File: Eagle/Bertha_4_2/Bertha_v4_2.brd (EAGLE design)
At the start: 100 x 84.6 mm, 117 parts, among them CON1 JACK_DC_BARREL, IC1 MCP1703DB, IC3 SN74LVC2G14, J1 RJ12RIGHTANGLE-I2C, J2 RJ12RIGHTANGLE-I2C, J7 22--02, Q1 BSP75, Q2 BSP75, Q3 BSP75, Q4 BSP75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

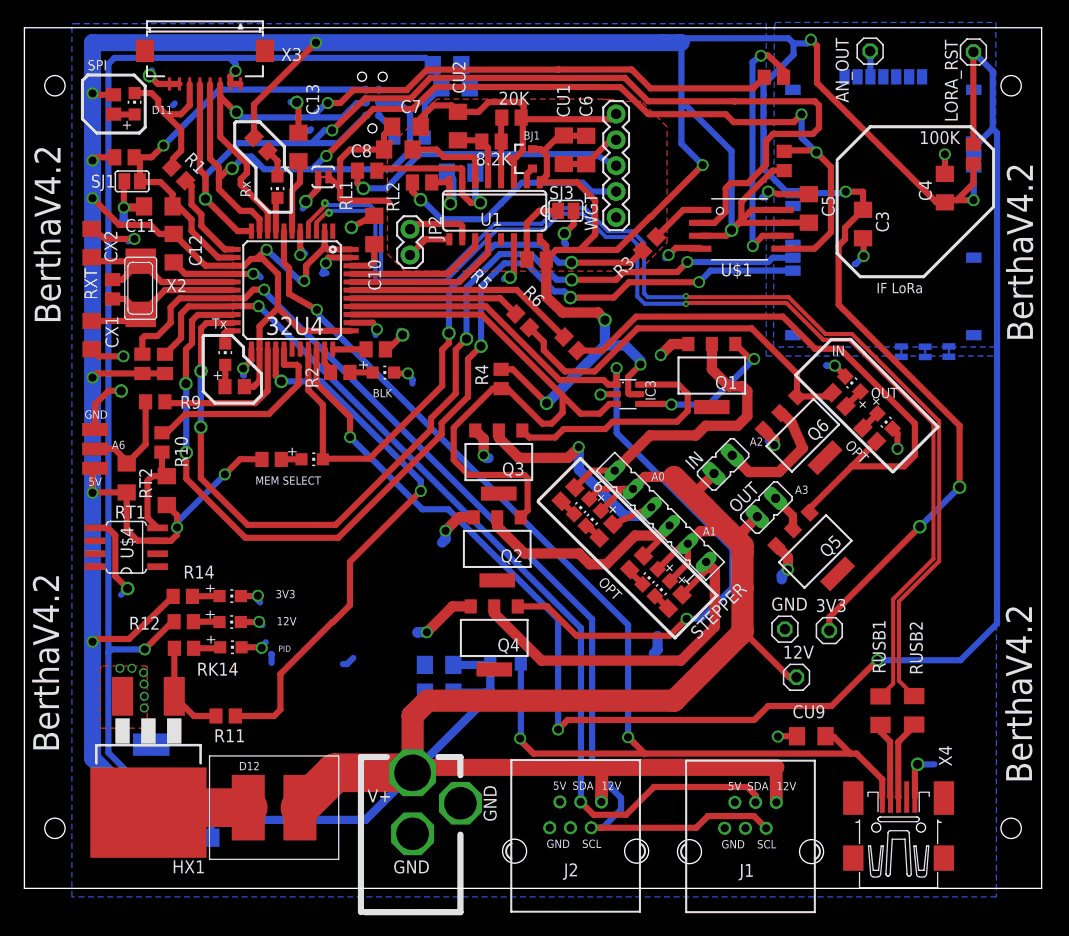
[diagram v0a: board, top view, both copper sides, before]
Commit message: corrected bioreactor board for microcircuitos (0.25mm clearance)
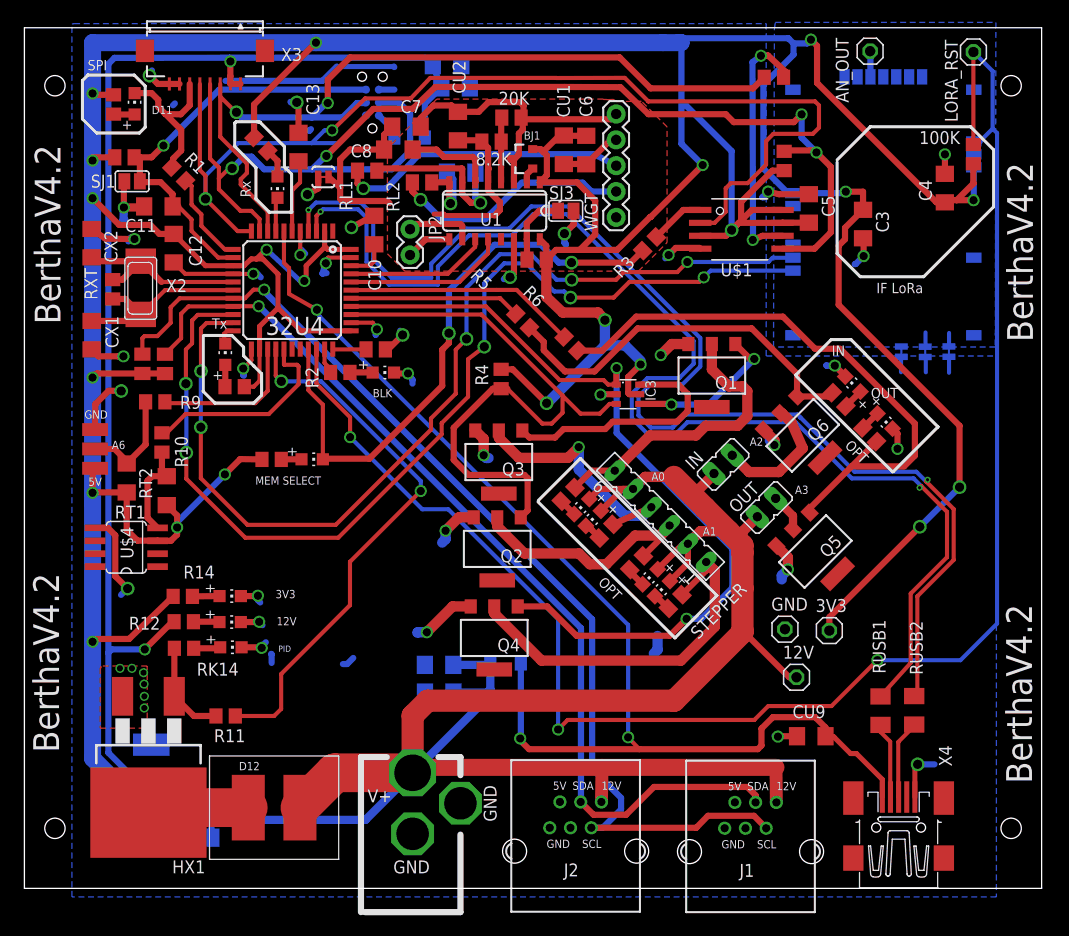
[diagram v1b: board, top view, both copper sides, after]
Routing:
- net GND: track 148.1 -> 170.2 mm
- net LGND: track 24.4 -> 35.7 mm
- net USB_N: track 112.3 -> 122.5 mm
- net USB_P: track 114.0 -> 124.0 mm
- net ANGND: track 5.01 -> 7.79 mm
- net SCK: track 80.3 -> 82.7 mm
- net N$23: track 26.2 -> 25.2 mm
